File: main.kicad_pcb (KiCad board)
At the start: 2 copper layers, 150 x 100 mm, 95 parts, among them J1 Screw_Terminal_01x10, J2 Screw_Terminal_01x02, J3 Conn_01x03, Q1 IRF540N, Q2 IRF540N, Q3 IRF540N, Q4 IRF540N, Q5 IRF540N, SW2 Switch_All, SW3 Switch1, SW4 Switch2, SW5 Switch3, SW6 Switch4, SW7 Switch5, U1 L7805, U2 ATmega328P-PU, U3 PC817, U4 PC817, U5 PC817, U6 PC817, U7 PC817, Y1 16mHz

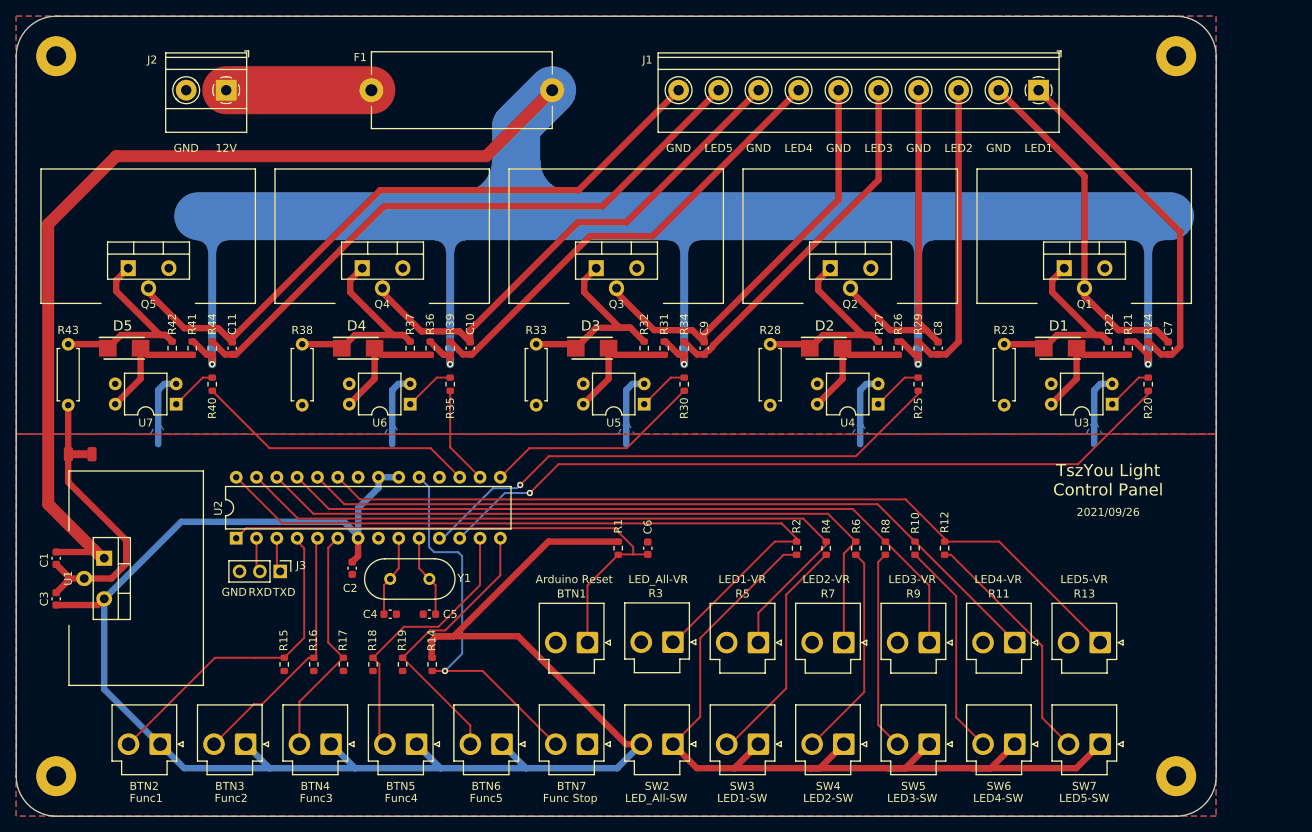
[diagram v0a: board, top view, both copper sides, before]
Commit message: [layout] modify screw size
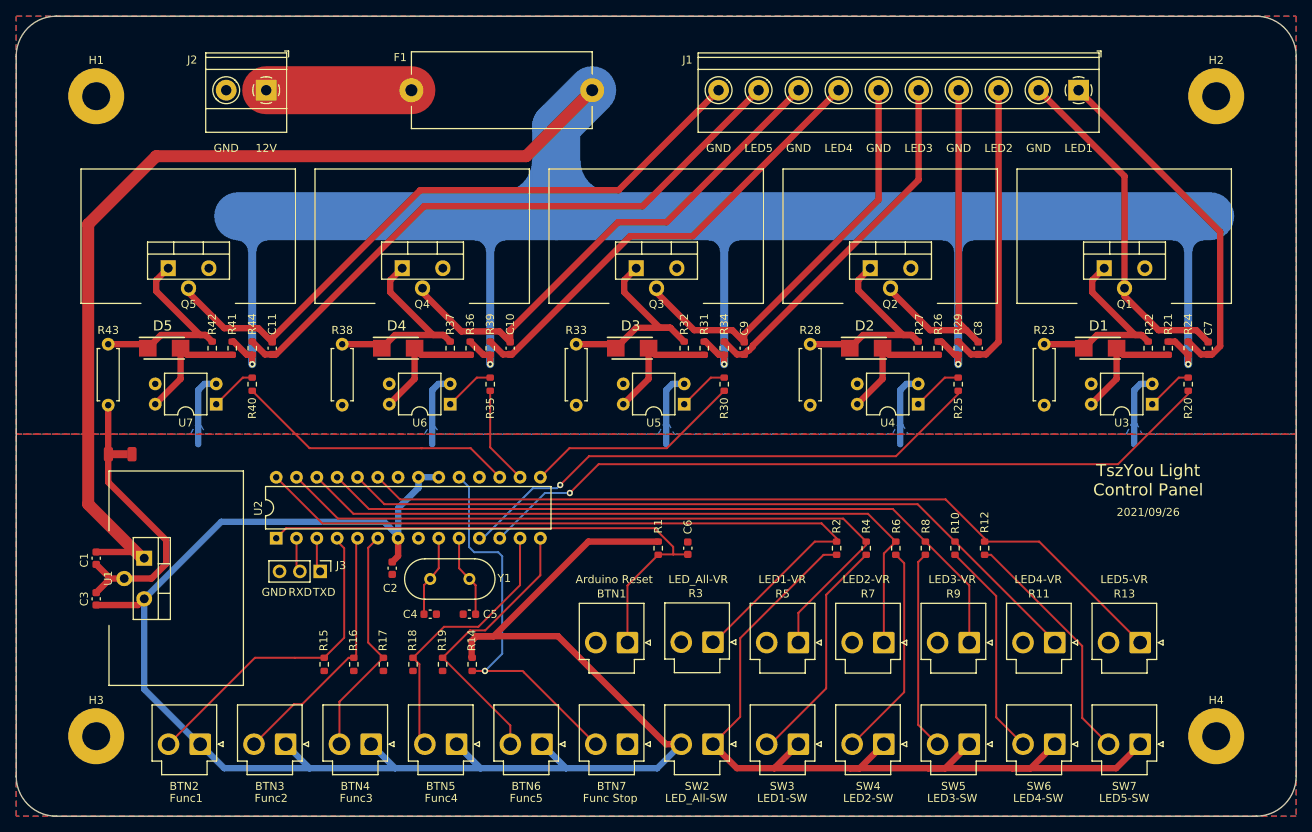
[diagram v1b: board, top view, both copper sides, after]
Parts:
- H1, H2, H3, H4: footprint MountingHole:MountingHole_2.5mm_Pad -> MountingHole:MountingHole_3.5mm_Pad
- moved H1 7.07 mm to (60.0, 60.0)
- moved H2 7.07 mm to (200.0, 60.0)
- moved H3 7.07 mm to (60.0, 140.0)
- moved H4 7.07 mm to (200.0, 140.0)
- moved BTN1 5.00 mm to (126.4, 128.3)
- moved BTN2 5.00 mm to (73.0, 141.0)
- moved BTN3 5.00 mm to (83.7, 141.0)
- moved BTN4 5.00 mm to (94.4, 141.0)
- moved BTN5 5.00 mm to (105.0, 141.0)
- moved BTN6 5.00 mm to (115.7, 141.0)
- moved BTN7 5.00 mm to (126.4, 141.0)
- moved C1 5.00 mm to (60.0, 117.8)
- moved C10 5.00 mm to (111.8, 91.5)
- moved C11 5.00 mm to (82.0, 91.5)
- moved C2 5.00 mm to (97.0, 119.0)
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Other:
- board size 150 x 100 mm -> 160 x 100 mm
